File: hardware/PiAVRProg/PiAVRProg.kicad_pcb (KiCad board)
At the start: 2 copper layers, 65 x 56 mm, 34 parts, among them J1 40HAT, SW2 MOM, U1 4066, U2 ATmega328P-PU

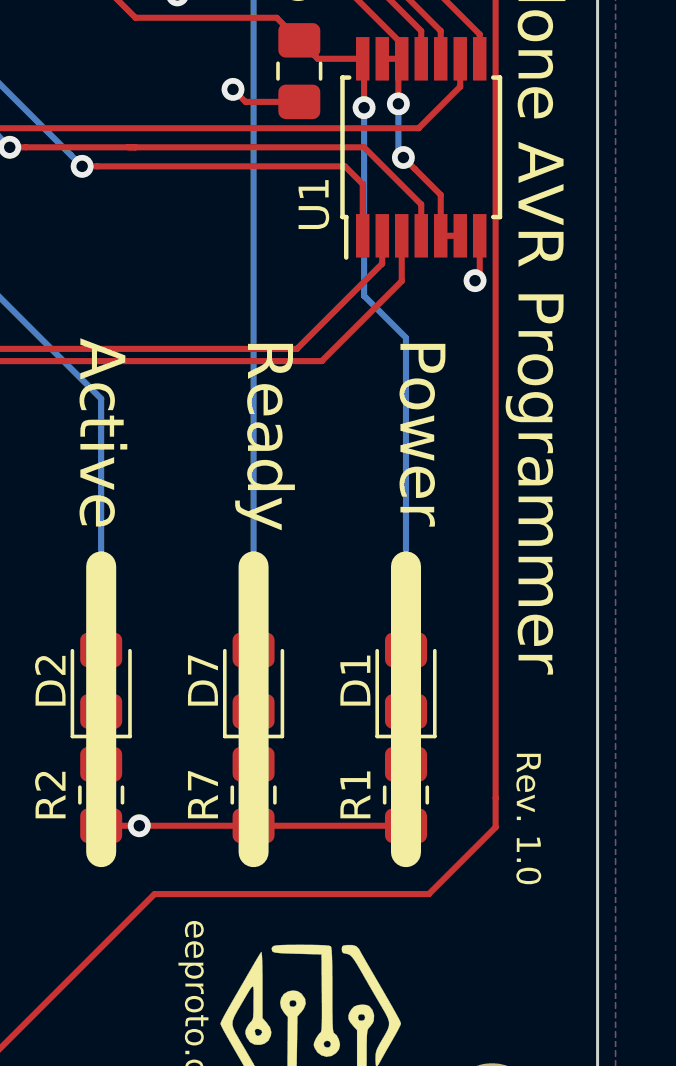
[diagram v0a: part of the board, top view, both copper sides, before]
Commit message: pin 1 indicator
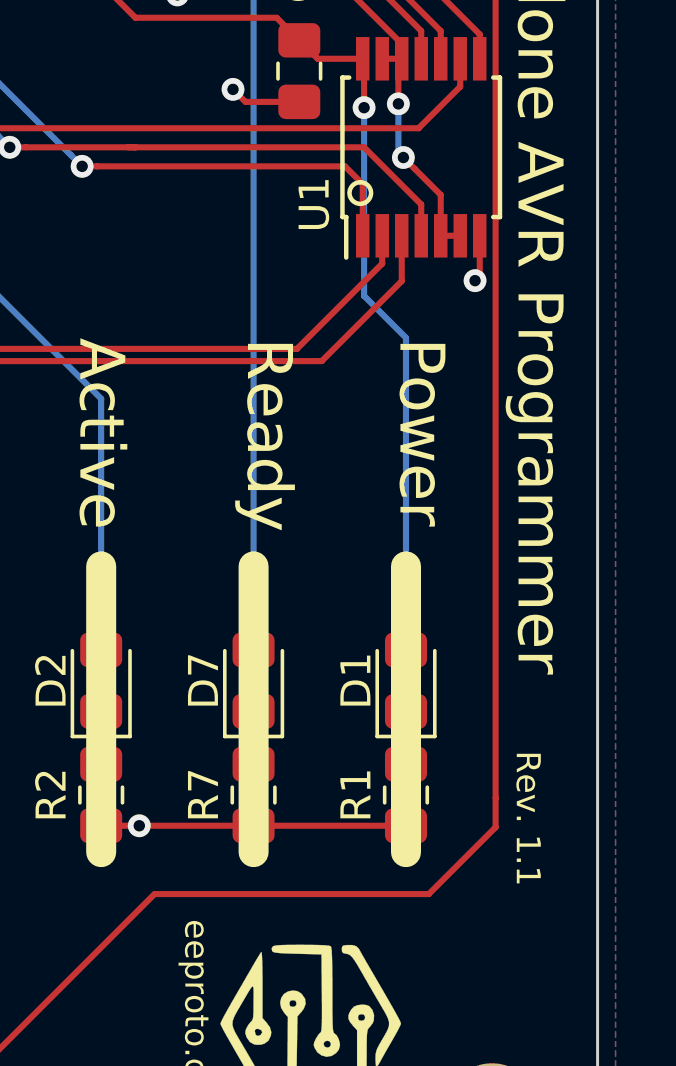
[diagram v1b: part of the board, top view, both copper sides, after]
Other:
- board text added: "Rev. 1.1"
- board text removed: "Rev. 1.0"
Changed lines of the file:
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@@
   (general
     (thickness 1.6)
-    (drawings 70)
+    (drawings 71)
     (tracks 243)
     (zones 0)
@@
   )
   (setup
-    (last_trace_width 0.2032)
+    (last_trace_width 0.1524)
     (user_trace_width 0.2032)
     (user_trace_width 0.508)
@@
       (xy 0.4191 0.20574) (xy 0.35814 0.29972) (xy 0.27686 0.37592) (xy 0.1778 0.4318)) (layer F.SilkS) (width 0.01))
   )
+  (gr_circle (center 135.636 82.804) (end 135.89 83.058) (layer F.SilkS) (width 0.15))
   (gr_text eeproto.com (at 130.175 110.49 270) (layer F.SilkS)
     (effects (font (size 0.8 0.8) (thickness 0.1)))
@@
     (effects (font (size 0.8 0.8) (thickness 0.1)))
   )
-  (gr_text "Rev. 1.0" (at 141.224 105.918 270) (layer F.SilkS)
+  (gr_text "Rev. 1.1" (at 141.224 105.918 270) (layer F.SilkS)
     (effects (font (size 0.8 0.8) (thickness 0.1)) (justify right))
   )

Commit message: kicad 8
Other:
- net class Default removed
- board text added: "CC BY-NC-SA 4.0 github.com/eeproto/PiAVRProg"
- board text removed: "CC-BY-SA 4.0 https://github.com/eeproto/PiAVRProg"
